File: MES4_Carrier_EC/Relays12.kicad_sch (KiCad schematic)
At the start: 32 parts, among them J6 RLY1 OUT, J7 RLY2 OUT, K1 SRD-5VDC-SL-A, K2 SRD-5VDC-SL-A, Q2 AO3400A, Q3 AO3400A, U2 INA226, U3 INA226

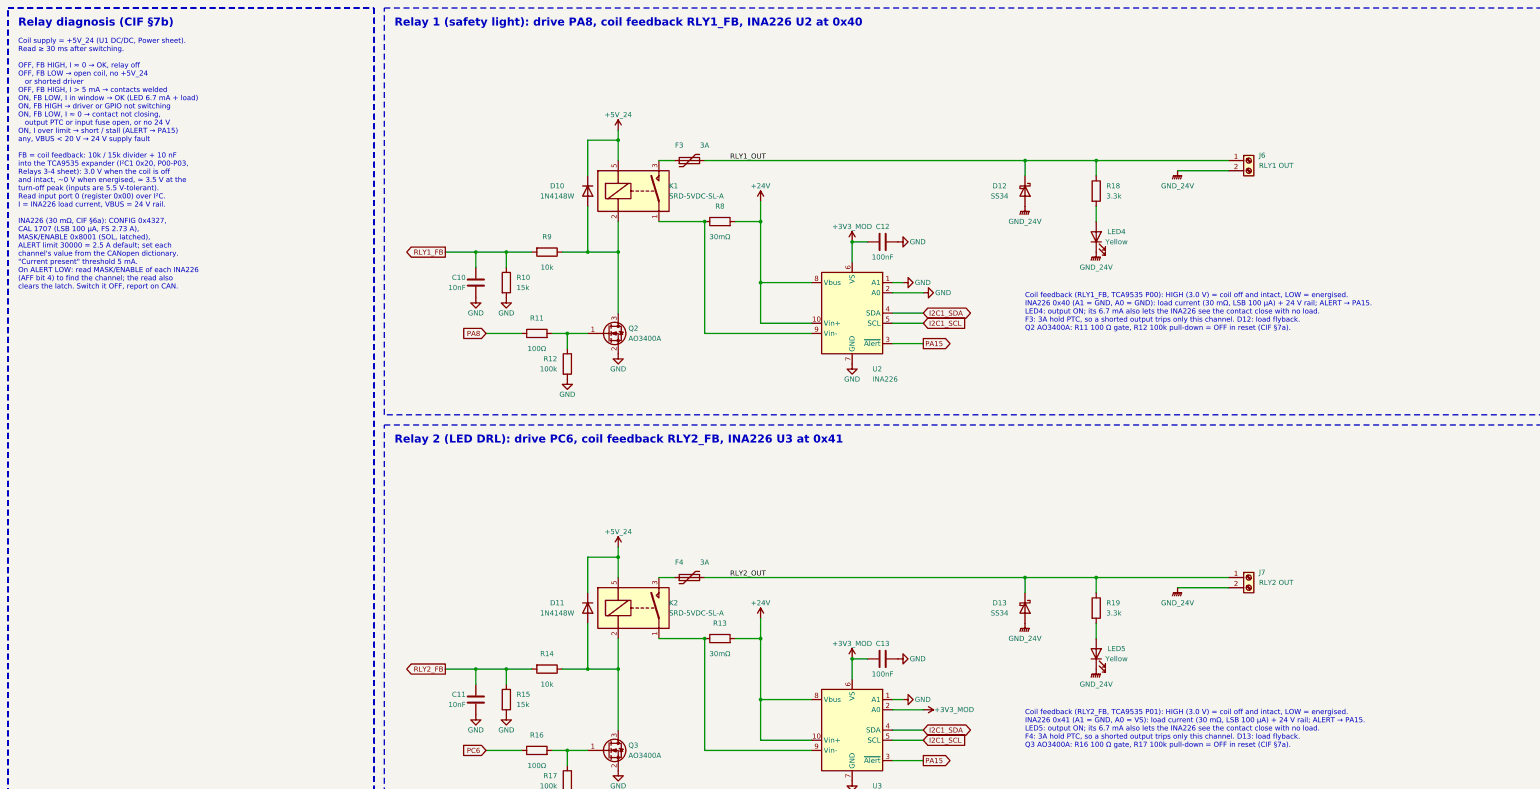
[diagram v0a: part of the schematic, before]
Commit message: Put relay coil feedback back on PA0-PA3 (MES4 GPIO standard)
All 14 module GPIOs now follow the MES4-CIF §2c table. The TCA9535 is
removed from the Relays 3-4 sheet and J1 fingers 43/45/47/49 drive the
relay 1-4 feedback dividers again. The winch relays are left undriven
(gate inputs no-connected, 100k pull-downs hold them off) until they
move to the TCA9535 + photoMOS design (HANDOFF.md step 2).

Removing U4 renumbers U5-U12 to U4-U11 and C15-C45 to C14-C44; the
README refs follow. Adds generator/checks.py (pin/pad, single-pin nets,
duplicate UUIDs, LCSC numbers), run by run.sh after ERC.

Co-Authored-By: Claude Opus 5.5 <noreply@anthropic.com>
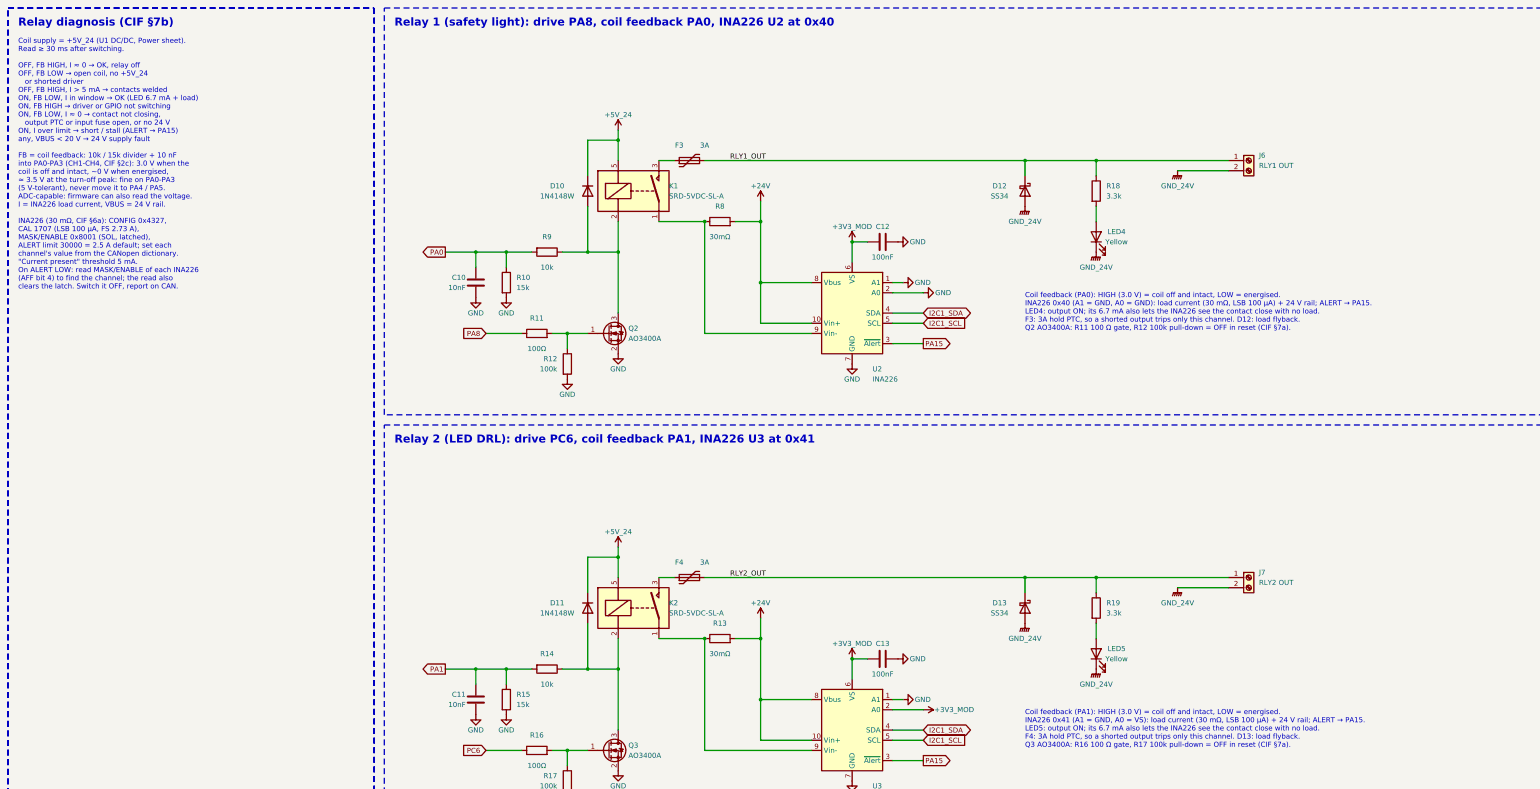
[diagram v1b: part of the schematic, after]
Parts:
- removed D12, D13: SS34, Diode_SMD:D_SMA, symbol Device:D_Schottky
- removed R10, R15: 15k, Resistor_SMD:R_0402_1005Metric, symbol Device:R
- removed R11, R16: 100Ω, Resistor_SMD:R_0402_1005Metric, symbol Device:R
- removed U2, U3: INA226, Package_SO:VSSOP-10_3x3mm_P0.5mm, symbol Sensor_Energy:INA226
- added J6: RLY1 OUT, MES4-Carrier-EC:CONN-TH_KF250NH-3.5-2P, symbol Connector:Screw_Terminal_01x02
- added J7: RLY2 OUT, MES4-Carrier-EC:CONN-TH_KF250NH-3.5-2P, symbol Connector:Screw_Terminal_01x02
- added Q2, Q3: AO3400A, Package_TO_SOT_SMD:SOT-23, symbol Transistor_FET:AO3400A
- added R12, R17: 100k, Resistor_SMD:R_0402_1005Metric, symbol Device:R
- added R13, R8: 30mΩ, Resistor_SMD:R_1206_3216Metric, symbol Device:R
- D12: renamed from J6; value RLY1 OUT -> SS34; footprint MES4-Carrier-EC:CONN-TH_KF250NH-3.5-2P -> Diode_SMD:D_SMA; symbol Connector:Screw_Terminal_01x02 -> Device:D_Schottky; LCSC C976556 -> C8678
- D13: renamed from J7; value RLY2 OUT -> SS34; footprint MES4-Carrier-EC:CONN-TH_KF250NH-3.5-2P -> Diode_SMD:D_SMA; symbol Connector:Screw_Terminal_01x02 -> Device:D_Schottky; LCSC C976556 -> C8678
- R10: renamed from R9; value 10k -> 15k; LCSC C25744 -> C25756
- R11: renamed from Q2; value AO3400A -> 100Ω; footprint Package_TO_SOT_SMD:SOT-23 -> Resistor_SMD:R_0402_1005Metric; symbol Transistor_FET:AO3400A -> Device:R; LCSC C20917 -> C25076
- R14: renamed from R17; value 100k -> 10k; LCSC C25741 -> C25744
- R15: renamed from R14; value 10k -> 15k; LCSC C25744 -> C25756
- R16: renamed from Q3; value AO3400A -> 100Ω; footprint Package_TO_SOT_SMD:SOT-23 -> Resistor_SMD:R_0402_1005Metric; symbol Transistor_FET:AO3400A -> Device:R; LCSC C20917 -> C25076
- R9: renamed from R12; value 100k -> 10k; LCSC C25741 -> C25744
- U2: renamed from R8; value 30mΩ -> INA226; footprint Resistor_SMD:R_1206_3216Metric -> Package_SO:VSSOP-10_3x3mm_P0.5mm; symbol Device:R -> Sensor_Energy:INA226; LCSC C5375399 -> C49851
- U3: renamed from R13; value 30mΩ -> INA226; footprint Resistor_SMD:R_1206_3216Metric -> Package_SO:VSSOP-10_3x3mm_P0.5mm; symbol Device:R -> Sensor_Energy:INA226; LCSC C5375399 -> C49851
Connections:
- net +24V: now also U2.10 (Vin+), U2.8 (Vbus), U3.10 (Vin+), U3.8 (Vbus), R13.2, R8.2; no longer U2.2, U3.2
- net +3V3_MOD: now also U2.6 (VS), U3.2 (A0), U3.6 (VS)
- net GND: now also R10.2, R15.2, U2.1 (A1), U2.2 (A0), U2.7 (GND), U3.1 (A1), U3.7 (GND), Q2.2 (S), Q3.2 (S), R12.2, R17.2; no longer R11.2 (S), R14.2, R16.2 (S), R9.2
- net GND_24V: now also J6.2 (Pin_2), J7.2 (Pin_2)
- net I2C1_SCL: now also U2.5 (SCL), U3.5 (SCL)
- net I2C1_SDA: now also U2.4 (SDA), U3.4 (SDA)
- net PA15: now also U2.3 (~{Alert}), U3.3 (~{Alert})
- net PA8: now also R11.1
- net PC6: now also R16.1
- net RLY1_OUT: now also J6.1 (Pin_1)
- net RLY2_OUT: now also J7.1 (Pin_1)
- net at K1.1: now also U2.9 (Vin-), R8.1; no longer U2.1
- net at D10.2 (A), K1.2: now also R9.1, Q2.3 (D); no longer R10.1, R11.3 (D)
- net at D11.2 (A), K2.2: now also R14.1, Q3.3 (D); no longer R15.1, R16.3 (D)
- net at K2.1: now also U3.9 (Vin-), R13.1; no longer U3.1
- net RLY1_FB renamed PA0
- net PA0: now also R10.1, R9.2; no longer R10.2
- net RLY2_FB renamed PA1
- net PA1: now also R14.2, R15.1; no longer R15.2
- new net: Q3.1 (G), R16.2, R17.1
- new net: Q2.1 (G), R11.2, R12.1
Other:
- note added: "Coil feedback (PA0): HIGH (3.0 V) = coil off and intact, LOW = energised. INA226 0x40 (A1 = GND, A0 = GND): load current (30 mΩ, LSB 100 µA) + 24 V rail; ALERT → PA15. LED4: output ON; its 6.7 mA also lets the INA226 see the contact close with no load. F3: 3A hold PTC, so a shorted output trips only this channel. D12: load flyback. Q2 AO3400A: R11 100 Ω gate, R12 100k pull-down = OFF in reset (CI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"
- note added: "Coil feedback (PA1): HIGH (3.0 V) = coil off and intact, LOW = energised. INA226 0x41 (A1 = GND, A0 = VS): load current (30 mΩ, LSB 100 µA) + 24 V rail; ALERT → PA15. LED5: output ON; its 6.7 mA also lets the INA226 see the contact close with no load. F4: 3A hold PTC, so a shorted output trips only this channel. D13: load flyback. Q3 AO3400A: R16 100 Ω gate, R17 100k pull-down = OFF in reset (CIF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"
- note added: "Relay 1 (safety light): drive PA8, coil feedback PA0, INA226 U2 at 0x40"
- note added: "Relay 2 (LED DRL): drive PC6, coil feedback PA1, INA226 U3 at 0x41"
- note removed: "Coil feedback (RLY1_FB, TCA9535 P00): HIGH (3.0 V) = coil off and intact, LOW = energised. INA226 0x40 (A1 = GND, A0 = GND): load current (30 mΩ, LSB 100 µA) + 24 V rail; ALERT → PA15. LED4: output ON; its 6.7 mA also lets the INA226 see the contact close with no load. F3: 3A hold PTC, so a shorted output trips only this channel. D12: load flyback. Q2 AO3400A: R11 100 Ω gate, R12 100k pull-down =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"
- note removed: "Coil feedback (RLY2_FB, TCA9535 P01): HIGH (3.0 V) = coil off and intact, LOW = energised. INA226 0x41 (A1 = GND, A0 = VS): load current (30 mΩ, LSB 100 µA) + 24 V rail; ALERT → PA15. LED5: output ON; its 6.7 mA also lets the INA226 see the contact close with no load. F4: 3A hold PTC, so a shorted output trips only this channel. D13: load flyback. Q3 AO3400A: R16 100 Ω gate, R17 100k pull-down = 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"
- note removed: "Relay 1 (safety light): drive PA8, coil feedback RLY1_FB, INA226 U2 at 0x40"
- note removed: "Relay 2 (LED DRL): drive PC6, coil feedback RLY2_FB, INA226 U3 at 0x41"
- moved on the sheet: R10, R14, R15, R9

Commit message: Drop relay coil feedback; winch on PA0/PA1, servo on USART2
User decision: free the four feedback pins instead of adding an I²C
expander. The Flasher template's 10k/15k/10 nF dividers are removed from
all relay channels and relay diagnosis is INA226-only. PA0/PA1 drive the
IM03GR winch relays again and PA2/PA3 carry the door servo UART
(USART2), so the SC16IS740 bridge, its crystal and caps, and the unused
TCA9535 code are removed. This deliberately differs from the MES4-CIF
§2c GPIO table; the GPIO map, root notes, README and HANDOFF say so.

189 parts, ERC clean, checks.py passes. README refs follow the
renumbering.

Co-Authored-By: Claude Opus 5.5 <noreply@anthropic.com>
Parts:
- removed C10, C11: 10nF, Capacitor_SMD:C_0402_1005Metric, symbol Device:C
- removed R10, R15: 15k, Resistor_SMD:R_0402_1005Metric, symbol Device:R
- removed R14, R9: 10k, Resistor_SMD:R_0402_1005Metric, symbol Device:R
- renumbered C12 to C10, C13 to C11, R12 to R10, R13 to R11, R16 to R12, R17 to R13, R18 to R14, R19 to R15, R11 to R9
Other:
- note added: "Coil supply = +5V_24 (U1 DC/DC, Power sheet). Read ≥ 30 ms after switching. OFF, I ≈ 0 → OK, relay off OFF, I > 5 mA → contacts welded or driver shorted ON, I in window → OK (LED 6.7 mA + load) ON, I ≈ 0 → relay not closing: open coil, driver or GPIO, no +5V_24, contact, output PTC or input fuse open, or no 24 V ON, I over limit → short / stall (ALERT → PA15) any, VBUS < 20 V → 24 V supply fault 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"
- note added: "No coil feedback: PA0-PA3 drive the winch and the servo UART; the INA226 does the diagnosis. INA226 0x40 (A1 = GND, A0 = GND): load current (30 mΩ, LSB 100 µA) + 24 V rail; ALERT → PA15. LED4: output ON; its 6.7 mA also lets the INA226 see the contact close with no load. F3: 3A hold PTC, so a shorted output trips only this channel. D12: load flyback. Q2 AO3400A: R9 100 Ω gate, R10 100k pull-down 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"
- note added: "No coil feedback: PA0-PA3 drive the winch and the servo UART; the INA226 does the diagnosis. INA226 0x41 (A1 = GND, A0 = VS): load current (30 mΩ, LSB 100 µA) + 24 V rail; ALERT → PA15. LED5: output ON; its 6.7 mA also lets the INA226 see the contact close with no load. F4: 3A hold PTC, so a shorted output trips only this channel. D13: load flyback. Q3 AO3400A: R12 100 Ω gate, R13 100k pull-down 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"
- note added: "Relay 1 (safety light): drive PA8, INA226 U2 at 0x40"
- note added: "Relay 2 (LED DRL): drive PC6, INA226 U3 at 0x41"
- note added: "Relay diagnosis (CIF §7b, INA226 only)"
- note removed: "Coil feedback (PA0): HIGH (3.0 V) = coil off and intact, LOW = energised. INA226 0x40 (A1 = GND, A0 = GND): load current (30 mΩ, LSB 100 µA) + 24 V rail; ALERT → PA15. LED4: output ON; its 6.7 mA also lets the INA226 see the contact close with no load. F3: 3A hold PTC, so a shorted output trips only this channel. D12: load flyback. Q2 AO3400A: R11 100 Ω gate, R12 100k pull-down = OFF in reset (CI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"
- note removed: "Coil feedback (PA1): HIGH (3.0 V) = coil off and intact, LOW = energised. INA226 0x41 (A1 = GND, A0 = VS): load current (30 mΩ, LSB 100 µA) + 24 V rail; ALERT → PA15. LED5: output ON; its 6.7 mA also lets the INA226 see the contact close with no load. F4: 3A hold PTC, so a shorted output trips only this channel. D13: load flyback. Q3 AO3400A: R16 100 Ω gate, R17 100k pull-down = OFF in reset (CIF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"
- note removed: "Coil supply = +5V_24 (U1 DC/DC, Power sheet). Read ≥ 30 ms after switching. OFF, FB HIGH, I ≈ 0 → OK, relay off OFF, FB LOW → open coil, no +5V_24 or shorted driver OFF, FB HIGH, I > 5 mA → contacts welded ON, FB LOW, I in window → OK (LED 6.7 mA + load) ON, FB HIGH → driver or GPIO not switching ON, FB LOW, I ≈ 0 → contact not closing, output PTC or input fuse open, or no 24 V ON, I over limit →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"
- note removed: "Relay 1 (safety light): drive PA8, coil feedback PA0, INA226 U2 at 0x40"
- note removed: "Relay 2 (LED DRL): drive PC6, coil feedback PA1, INA226 U3 at 0x41"
- note removed: "Relay diagnosis (CIF §7b)"

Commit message: Address design review R1: INA236, J15 polarity, review fixes
M1: U2-U5 are now TI INA236AIDDFR (C5443912, 50 V abs max, TSOT-23-8)
instead of the INA226 (40 V), since the SMBJ30A clamps at up to 48.4 V.
A project INA236 symbol keeps the INA226 body so the Flasher relay
wiring lands on the same pins; A1 and VBUS are gone (bus read on IN-),
addresses 0x40-0x43 via A0 = GND / VS / SDA / SCL. Same CONFIG / CAL /
MASK / ALERT values; notes give the 1.6 mV bus LSB and Device ID.
M3: J15 servo 24 V is pin 1 = +24 V like every power terminal.
L4: R38 servo RX series resistor 1k (limits PA3 back-feed).
L2: "current present" threshold 3 mA. L6: Power notes use 13 A / 2.2 W.
M2 / L5: silkscreen notes for "5V LOAD CELL - NEVER 24V" and
"CAN - NOT ETHERNET" (no keyed connector, by choice).
RJ45 1x4 footprint rebuilt from the HCTL drawing (14.0 mm ports,
Ø1.5 shield and Ø3.2 peg positions); U1 / U9 / U10 checked against the
JLC library and YLPTEC drawing. HANDOFF gains the review status table
and a layout checklist.

Co-Authored-By: Claude Opus 5.5 <noreply@anthropic.com>
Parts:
- U2, U3: value INA226 -> INA236; footprint Package_SO:VSSOP-10_3x3mm_P0.5mm -> Package_TO_SOT_SMD:TSOT-23-8; symbol Sensor_Energy:INA226 -> MES4-Carrier-EC:INA236; LCSC C49851 -> C5443912
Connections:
- net +24V: now also U2.1 (IN+), U3.1 (IN+); no longer U2.10 (Vin+), U2.8 (Vbus), U3.10 (Vin+), U3.8 (Vbus)
- net +3V3_MOD: now also U2.4 (VS), U3.4 (VS), U3.7 (A0); no longer U2.6 (VS), U3.2 (A0), U3.6 (VS)
- net GND: now also U2.3 (GND), U3.3 (GND); no longer U2.1 (A1), U2.2 (A0), U3.1 (A1), U3.7 (GND)
- net I2C1_SDA: now also U2.6 (SDA), U3.6 (SDA); no longer U2.4 (SDA), U3.4 (SDA)
- net PA15: now also U2.8 (~{ALERT}), U3.8 (~{ALERT}); no longer U2.3 (~{Alert}), U3.3 (~{Alert})
- net at K1.1, R8.1: now also U2.2 (IN-); no longer U2.9 (Vin-)
- net at K2.1, R11.1: now also U3.2 (IN-); no longer U3.9 (Vin-)
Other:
- note added: "Coil supply = +5V_24 (U1 DC/DC, Power sheet). Read ≥ 30 ms after switching. OFF, I ≈ 0 → OK, relay off OFF, I > 3 mA → contacts welded or driver shorted ON, I in window → OK (LED 6.7 mA + load) ON, I ≈ 0 → relay not closing: open coil, driver or GPIO, no +5V_24, contact, output PTC or input fuse open, or no 24 V ON, I over limit → short / stall (ALERT → PA15) any, VBUS < 20 V → 24 V supply fault 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"
- note added: "No coil feedback: PA0-PA3 drive the winch and the servo UART; the INA236 does the diagnosis. INA236 0x40 (A0 = GND): load current (30 mΩ, LSB 100 µA) + 24 V rail (read on IN-); ALERT → PA15. LED4: output ON; its 6.7 mA also lets the INA236 see the contact close with no load. F3: 3A hold PTC, so a shorted output trips only this channel. D12: load flyback. Q2 AO3400A: R9 100 Ω gate, R10 100k pull-d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"
- note added: "No coil feedback: PA0-PA3 drive the winch and the servo UART; the INA236 does the diagnosis. INA236 0x41 (A0 = VS): load current (30 mΩ, LSB 100 µA) + 24 V rail (read on IN-); ALERT → PA15. LED5: output ON; its 6.7 mA also lets the INA236 see the contact close with no load. F4: 3A hold PTC, so a shorted output trips only this channel. D13: load flyback. Q3 AO3400A: R12 100 Ω gate, R13 100k pull-d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"
- note added: "Relay 1 (safety light): drive PA8, INA236 U2 at 0x40"
- note added: "Relay 2 (LED DRL): drive PC6, INA236 U3 at 0x41"
- note added: "Relay diagnosis (CIF §7b, INA236 only)"
- note removed: "Coil supply = +5V_24 (U1 DC/DC, Power sheet). Read ≥ 30 ms after switching. OFF, I ≈ 0 → OK, relay off OFF, I > 5 mA → contacts welded or driver shorted ON, I in window → OK (LED 6.7 mA + load) ON, I ≈ 0 → relay not closing: open coil, driver or GPIO, no +5V_24, contact, output PTC or input fuse open, or no 24 V ON, I over limit → short / stall (ALERT → PA15) any, VBUS < 20 V → 24 V supply fault 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"
- note removed: "No coil feedback: PA0-PA3 drive the winch and the servo UART; the INA226 does the diagnosis. INA226 0x40 (A1 = GND, A0 = GND): load current (30 mΩ, LSB 100 µA) + 24 V rail; ALERT → PA15. LED4: output ON; its 6.7 mA also lets the INA226 see the contact close with no load. F3: 3A hold PTC, so a shorted output trips only this channel. D12: load flyback. Q2 AO3400A: R9 100 Ω gate, R10 100k pull-down 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"
- note removed: "No coil feedback: PA0-PA3 drive the winch and the servo UART; the INA226 does the diagnosis. INA226 0x41 (A1 = GND, A0 = VS): load current (30 mΩ, LSB 100 µA) + 24 V rail; ALERT → PA15. LED5: output ON; its 6.7 mA also lets the INA226 see the contact close with no load. F4: 3A hold PTC, so a shorted output trips only this channel. D13: load flyback. Q3 AO3400A: R12 100 Ω gate, R13 100k pull-down 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"
- note removed: "Relay 1 (safety light): drive PA8, INA226 U2 at 0x40"
- note removed: "Relay 2 (LED DRL): drive PC6, INA226 U3 at 0x41"
- note removed: "Relay diagnosis (CIF §7b, INA226 only)"

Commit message: Import all footprints into the PCB; TI land pattern for the INA236
MES4_Carrier_EC.kicad_pcb: all 190 footprints and 146 nets, grouped by
schematic sheet below the 200 x 100 mm outline, ready to place. Each
footprint carries its symbol path (F8 updates it instead of duplicating),
nets, LCSC number and BOM setting. DRC: schematic parity 0 issues,
0 clearance errors; 450 unconnected items (unrouted).

generator/import_footprints.py does the one-time import with KiCad's
pcbnew Python and refuses a board that already has footprints.

U2-U5 INA236 now use the project footprint TSOT-23-8_TI_DDF (TI DDF0008A
land pattern: 1.05 x 0.45 mm pads, rows 2.6 mm apart). KiCad's generic
TSOT-23-8 left 0.15 mm pad gaps against the 0.2 mm clearance.

.kicad_pro regenerated: KiCad had rewritten it on exit and dropped the
Winch_48V net class. HANDOFF notes the import, the footprint and the fix.

Co-Authored-By: Claude Opus 5.5 <noreply@anthropic.com>
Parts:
- U2, U3: footprint Package_TO_SOT_SMD:TSOT-23-8 -> MES4-Carrier-EC:TSOT-23-8_TI_DDF
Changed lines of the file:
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@@
 			(effects (font (size 1.27 1.27)) (justify left))
 		)
-		(property "Footprint" "Package_TO_SOT_SMD:TSOT-23-8"
+		(property "Footprint" "MES4-Carrier-EC:TSOT-23-8_TI_DDF"
 			(at 226.06 96.52 0)
 			(effects (font (size 1.27 1.27)) (hide yes))
@@
 			(effects (font (size 1.27 1.27)) (justify left))
 		)
-		(property "Footprint" "Package_TO_SOT_SMD:TSOT-23-8"
+		(property "Footprint" "MES4-Carrier-EC:TSOT-23-8_TI_DDF"
 			(at 226.06 200.66 0)
 			(effects (font (size 1.27 1.27)) (hide yes))

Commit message: One ground and a 4-layer board
- GND_24V merged into GND (ONE_GND in gen.py): every GND_24V power symbol
  becomes GND, net tie NT1 left out, notes reworded. Symbol UUIDs unchanged,
  so every footprint keeps its link.
- 4 layers, JLC04161H-7628 stackup (1.6 mm, ENIG): Top Signal / GND plane
  (In1) / +24V plane (In2) / Bottom Signal.
- Net classes: Out_3A (1.5 mm) for +24V_SRV, +5V_SCR, VBUS_SCR; +24V_AUX to
  24V_Power; +5V_SRV, +9V_IMU, IMU_9V to Power; INA236 shunt pattern fixed
  (Net-(U*-IN-)).
- J1's NPTH holes back to F&B.Cu as in its library footprint.

ERC 0, checks passed, DRC 11 silkscreen warnings, schematic parity clean.

Co-Authored-By: Claude Opus 5.5 <noreply@anthropic.com>
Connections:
- net GND_24V is gone; now on net GND: D12.2 (A), D13.2 (A), J6.2 (Pin_2), J7.2 (Pin_2), LED4.1 (K), LED5.1 (K)
